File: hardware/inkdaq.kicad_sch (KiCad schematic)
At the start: 0 parts

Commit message: create HSFPAR004A symbol and footprint
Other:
- company: (none) -> Stratos Thivaios
- title: (none) -> InkDAQ - Pen sensor board
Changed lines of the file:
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@@
 	(generator_version "9.0")
 	(paper "A4")
+	(title_block
+		(title "InkDAQ - Pen sensor board")
+		(date "2026-03-01")
+		(rev "1.0")
+		(company "Stratos Thivaios")
+		(comment 1 "CERN Open Hardware License v2 - Strongly Reciprocal")
+		(comment 2 "Copyright © 2026 Stratos Thivaios")
+		(comment 3 "github.com/sthivaios/inkdaq")
+		(comment 4 "InkDAQ - An opensource data acquisition system for handwriting telemetry")
+	)
 	(sheet_instances
 		(path "/"

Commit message: create very rough FPC
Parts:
- added B1: ~, inkdaq_footprints:HSFPAR004A, symbol inkdaq_symbols:HSFPAR004A
- added R1: 2.05k, Resistor_SMD:R_0201_0603Metric, symbol Device:R
- added U1: INA333xxDRG, Package_SON:WSON-8-1EP_3x3mm_P0.5mm_EP1.45x2.4mm, symbol Amplifier_Instrumentation:INA333xxDRG
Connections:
- new net: R1.1, U1.1 (Rg)
- new net: R1.2, U1.8 (Rg)
- new net AMP_OUT: U1.6
- new net GND: B1.3 (GND), B1.5 (GND), U1.4 (V-), U1.5 (Ref), U1.9 (EP)
- new net HSFPAR_V_NEG: B1.2 (V2_NO), U1.2 (-)
- new net HSFPAR_V_POS: B1.4 (V1), U1.3 (+)
- new net VDD: B1.1 (VDD), U1.7 (V+)

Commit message: add LCSC part numbers
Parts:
- B1: LCSC (none) -> C470800
- R1: LCSC (none) -> C851698
- U1: LCSC (none) -> C2057429
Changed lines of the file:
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@@
+			)
+		)
+		(property "LCSC" "C2057429"
+			(at 146.05 104.14 0)
+			(effects
+				(font
+					(size 1.27 1.27)
+				)
+				(hide yes)
 			)
 		)
@@
 		(property "Description" "Resistor"
 			(at 133.35 104.14 0)
+			(effects
+				(font
+					(size 1.27 1.27)
+				)
+				(hide yes)
+			)
+		)
+		(property "LCSC" "C851698"
+			(at 133.35 104.14 90)
 			(effects
 				(font
@@
 			(effects
 				(font
+					(size 1.27 1.27)
+				)
+				(hide yes)
+			)
+		)
+		(property "LCSC" "C470800"
+			(at 88.9 115.57 0)
+			(effects
+				(font

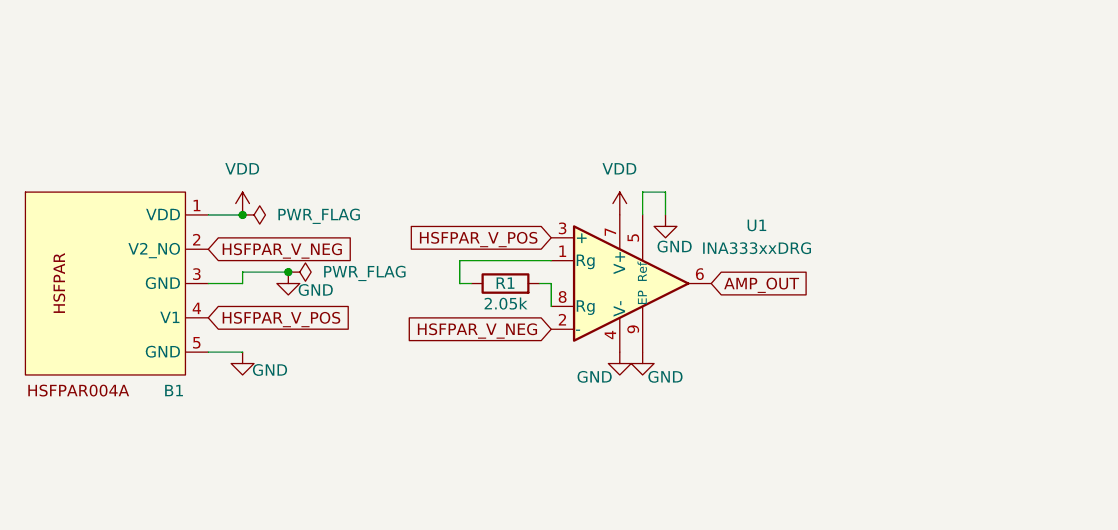
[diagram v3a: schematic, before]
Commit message: remove INA333 from schematic; add wire pads
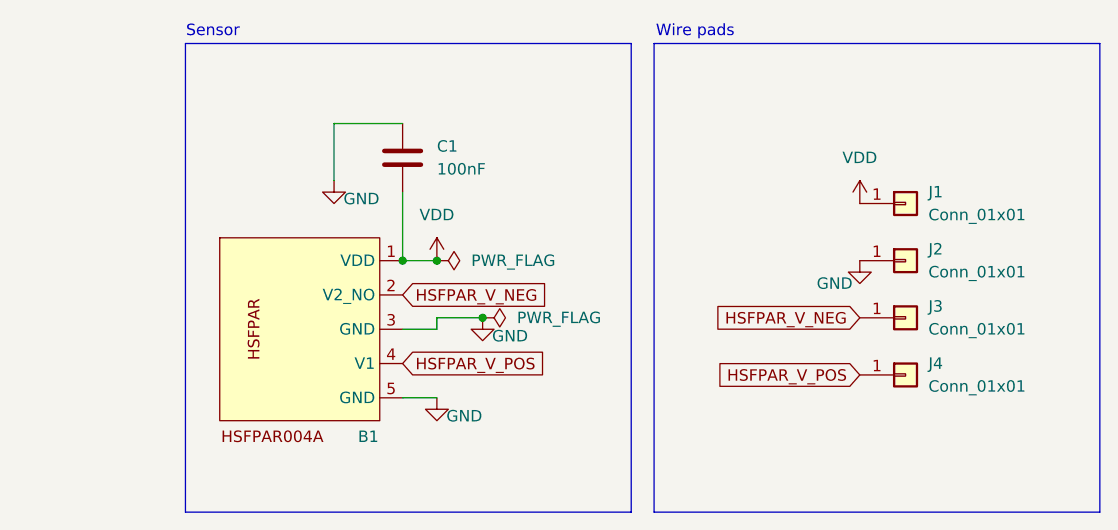
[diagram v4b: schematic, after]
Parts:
- removed R1: 2.05k, Resistor_SMD:R_0201_0603Metric, symbol Device:R
- removed U1: INA333xxDRG, Package_SON:WSON-8-1EP_3x3mm_P0.5mm_EP1.45x2.4mm, symbol Amplifier_Instrumentation:INA333xxDRG
- added C1: 100nF, symbol Device:C
- added J1, J2, J3, J4: Conn_01x01, Connector_Wire:SolderWire-0.1sqmm_1x01_D0.4mm_OD1mm, symbol Connector_Generic:Conn_01x01
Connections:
- net GND: now also C1.1, J2.1 (Pin_1)
- net HSFPAR_V_NEG: now also J3.1 (Pin_1)
- net HSFPAR_V_POS: now also J4.1 (Pin_1)
- net VDD: now also C1.2, J1.1 (Pin_1)
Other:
- note added: "Sensor"
- note added: "Wire pads"
- moved on the sheet: B1

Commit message: set footprint for HSFPAR's decoupling cap C1
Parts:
- C1: footprint (none) -> Capacitor_SMD:C_0201_0603Metric
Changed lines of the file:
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@@
 			)
 		)
-		(property "Footprint" ""
+		(property "Footprint" "Capacitor_SMD:C_0201_0603Metric"
 			(at 122.8852 93.98 0)
 			(effects

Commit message: create 1mm square smd wire pad; use it in schematic for wires
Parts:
- J1, J2, J3, J4: footprint Connector_Wire:SolderWire-0.1sqmm_1x01_D0.4mm_OD1mm -> inkdaq_footprints:WirePad_1mm_Square
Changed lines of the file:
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@@
 			)
 		)
-		(property "Footprint" "Connector_Wire:SolderWire-0.1sqmm_1x01_D0.4mm_OD1mm"
+		(property "Footprint" "inkdaq_footprints:WirePad_1mm_Square"
 			(at 177.8 101.6 0)
 			(effects
@@
 		(on_board yes)
 		(dnp no)
-		(fields_autoplaced yes)
 		(property "Reference" "J4"
 			(at 180.34 113.0299 0)
@@
 			)
 		)
-		(property "Footprint" "Connector_Wire:SolderWire-0.1sqmm_1x01_D0.4mm_OD1mm"
-			(at 177.8 114.3 0)
+		(property "Footprint" "inkdaq_footprints:WirePad_1mm_Square"
+			(at 177.8 120.904 0)
 			(effects
 				(font
@@
 			)
 		)
-		(property "Footprint" "Connector_Wire:SolderWire-0.1sqmm_1x01_D0.4mm_OD1mm"
+		(property "Footprint" "inkdaq_footprints:WirePad_1mm_Square"
 			(at 177.8 107.95 0)
 			(effects
@@
 			)
 		)
-		(property "Footprint" "Connector_Wire:SolderWire-0.1sqmm_1x01_D0.4mm_OD1mm"
+		(property "Footprint" "inkdaq_footprints:WirePad_1mm_Square"
 			(at 177.8 95.25 0)
 			(effects
